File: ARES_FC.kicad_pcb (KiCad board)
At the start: 2 copper layers, 57.2 x 57.2 mm, 86 parts, among them J1 SWD, J2 TYPE-C-31-M-12, J3 FC_M/P, J4 5V, J5 GND, J6 FC_RF, J7 Conn_01x04_Pin, J8 Conn_01x04_Pin, U1 STM32F401CCU6, U2 AMS1117-3.3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

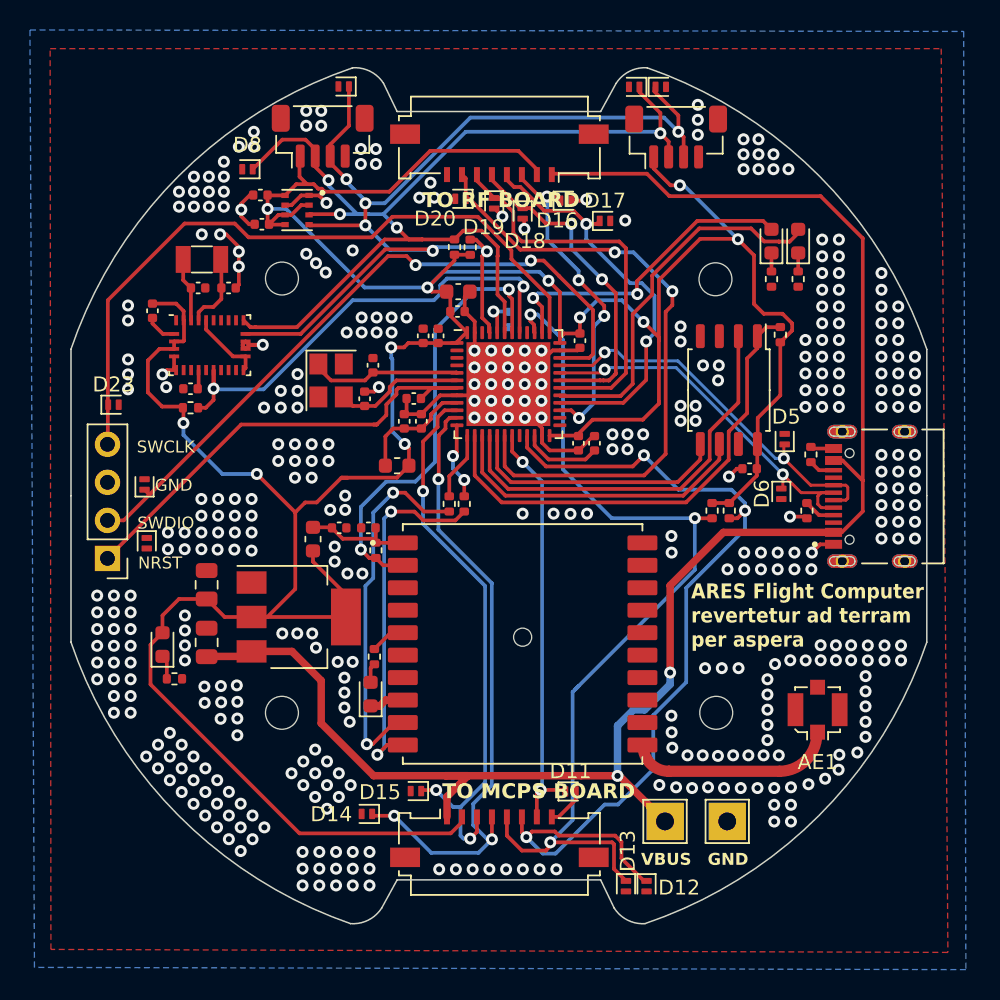
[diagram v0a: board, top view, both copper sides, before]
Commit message: changed GPS antenna tracewidth to match impedance and added stitches
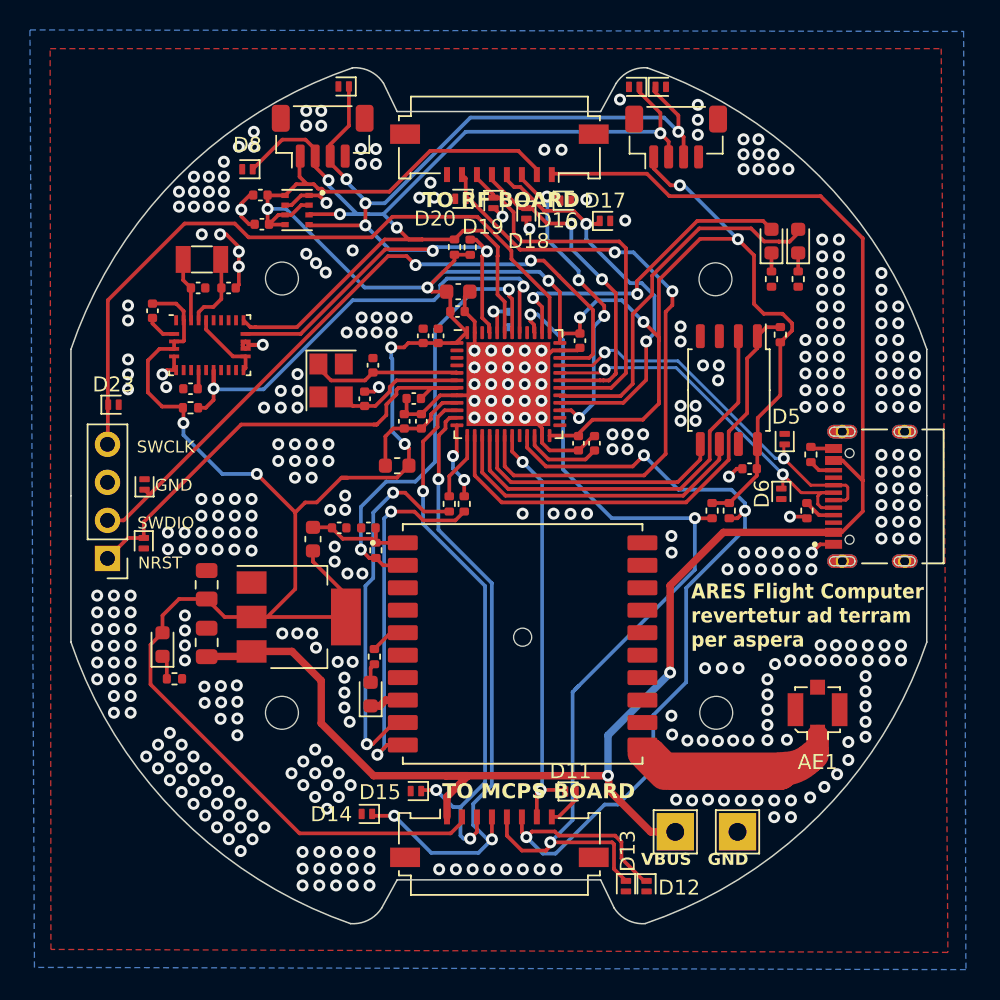
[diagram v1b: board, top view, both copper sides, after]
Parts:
- moved J4 0.98 mm to (161.7, 122.0)
- moved J5 0.98 mm to (165.9, 122.0)
- moved D18 0.25 mm to (151.8, 80.7)
- moved D21 0.20 mm to (126.2, 102.7)
- moved D19 0.06 mm to (149.6, 80.0)
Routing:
- net Net-(AE1-A): track 7.39 -> 17.3 mm
- net VBUS: track 115.4 -> 116.8 mm
- net GND: track 66.2 -> 65.5 mm, vias 398 -> 396
- net /NRST: track 31.8 -> 32.3 mm

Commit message: rerouted BOOT0 pull-down (was on back side)
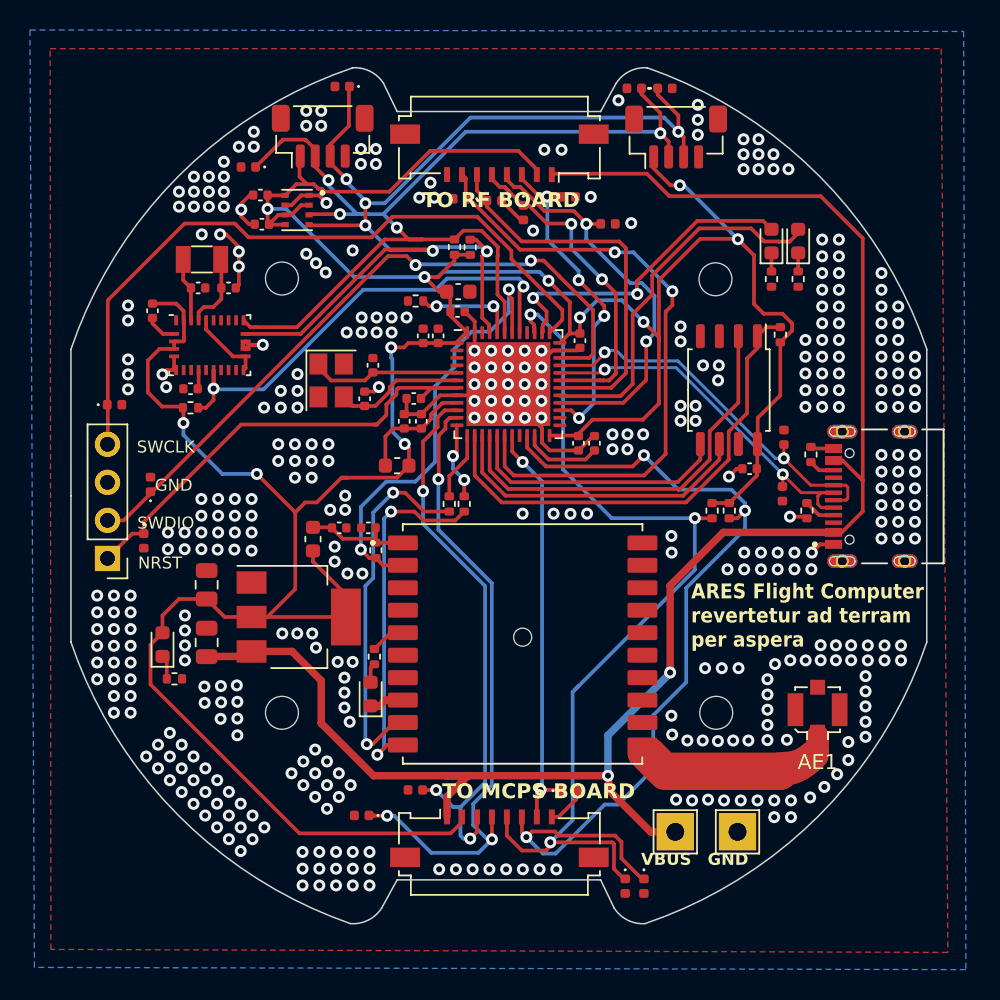
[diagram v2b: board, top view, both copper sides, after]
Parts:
- D10, D11, D12, D13, D14, D15, D16, D17, D18, D19, D20, D21, D22, D23, D5, D6, D7, D8, D9: footprint Diode_SMD:D_SOD-882 -> Diode_SMD:D_0402_1005Metric
- R14: moved to F.Cu
- moved R14 6.37 mm to (144.4, 86.5), turned to 0 degrees
- moved D22 0.40 mm to (126.7, 98.8)
- moved D14 0.36 mm to (140.8, 120.8)
- moved D16 0.31 mm to (154.6, 79.5)
- moved D10 0.29 mm to (161.1, 72.3)
- moved D17 0.28 mm to (157.2, 81.3)
- moved D18 0.21 mm to (151.6, 80.6)
- moved D12 0.17 mm to (159.7, 125.6)
- moved D8 0.16 mm to (133.2, 77.5)
- moved D19 0.16 mm to (149.7, 79.8), turned to 0 degrees
- moved D21 0.16 mm to (126.2, 102.5)
- moved D5 0.13 mm to (169.0, 95.6)
- moved D7 0.10 mm to (139.5, 72.2)
- moved D9 0.10 mm to (159.0, 72.3)
- moved D11 0.10 mm to (154.7, 119.2)
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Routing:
- net Net-(U1-BOOT0): track 2.58 -> 6.75 mm, vias 1 -> 2
- net /RX_RADIO: track 22.0 -> 22.8 mm
- net /SWCLK: track 47.1 -> 47.8 mm
- net GND: track 65.5 -> 64.8 mm, vias 396 -> 395
- net /GPS_NRST: track 30.2 -> 29.5 mm

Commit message: WINTER 2026 ARES FC ORDER
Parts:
- D10, D11, D12, D13, D14, D15, D16, D17, D18, D19, D20, D21, D22, D23, D5, D6, D7, D8, D9: footprint Diode_SMD:D_0402_1005Metric -> Diode_SMD:D_SOD-882
- moved D22 0.49 mm to (126.3, 99.1)
- moved D15 0.43 mm to (143.9, 119.2)
- moved D20 0.35 mm to (147.1, 79.7)
- moved D18 0.25 mm to (151.6, 80.8)
- moved D10 0.16 mm to (160.9, 72.3)
- moved D16 0.16 mm to (154.6, 79.7)
- moved D12 0.15 mm to (159.8, 125.6)
- moved D21 0.12 mm to (126.2, 102.4)
- moved D7 0.10 mm to (139.6, 72.2)
- moved D8 0.05 mm to (133.2, 77.6)
- moved D14 0.05 mm to (140.8, 120.9)
- moved D5 0.05 mm to (169.0, 95.7)
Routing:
- net GND: track 64.8 -> 62.5 mm, vias 395 -> 397
- net /SWDIO: track 47.1 -> 47.9 mm
- net /MOTOR_SCL: track 62.0 -> 61.4 mm
- net /RADIO_NRST: track 42.8 -> 43.3 mm
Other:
- board text added: "5V"
- board text removed: "VBUS"
